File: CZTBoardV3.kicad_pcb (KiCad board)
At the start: 2 copper layers, 80 x 100 mm, 34 parts, among them IC1 LD117AS, IC2 LD117AS, U1 ORBOTECH_OMS40G256, U2 DS90LV031, U3 DS90LV032, X1 W237-102, X2 W237-102, X3 W237-103, X4 W237-102, X5 W237-102

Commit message: new layout
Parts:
- removed the X1 at (105.4, 41.9)

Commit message: added side panel
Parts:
- removed C5: C5, CZTBoardV3:C0805K
- removed R7, R8: 0, CZTBoardV3:R1206
- added C10: 0.0123uF, CZTBoardV3:C0805K, F.Cu at (144.5, 64.5)
- added C11: 0.1uF, CZTBoardV3:C0805K, F.Cu at (135.9, 66.6)
- added C12: 0.1uF, CZTBoardV3:C0805K, F.Cu at (149.1, 52.9)
- added C13: 4.7uF, CZTBoardV3:C0805K, F.Cu at (148.9, 55.9)
- added C14: 4.7uF, CZTBoardV3:C0805K, F.Cu at (142.9, 61.9)
- added C15: 0.1uF, CZTBoardV3:C0805K, F.Cu at (140.2, 65.8)
- added C16: 0.1uF, CZTBoardV3:C0805K, F.Cu at (153.4, 52.9)
- added C17: 4.7uF, CZTBoardV3:C0805K, F.Cu at (147.2, 59.3)
- added C18: 4.7uF, CZTBoardV3:C0805K, F.Cu at (153.2, 55.5)
- added C19: 0.1uF, CZTBoardV3:C0805K, F.Cu at (147.2, 61.9)
- added C20: 0.1uF, CZTBoardV3:C0805K, F.Cu at (142.9, 59.3)
- added C21: 4.7uF, CZTBoardV3:C0805K, F.Cu at (151.5, 58.5)
- added C22: 4.7uF, CZTBoardV3:C0805K, F.Cu at (151.5, 61.1)
- added L1: 40uH, Inductor_SMD:L_1206_3216Metric, F.Cu at (137.9, 62.8)
- added L2: 100uH, Inductor_SMD:L_1206_3216Metric, F.Cu at (137.9, 59.3)
- added L3: 100uH, Inductor_SMD:L_1206_3216Metric, F.Cu at (143.9, 56.3)
- added R20: 470k, CZTBoardV3:R1206, F.Cu at (138.0, 56.1)
- added R21: 10E, CZTBoardV3:R1206, F.Cu at (144.0, 53.1)
- added R22: 10E, CZTBoardV3:R1206, F.Cu at (138.0, 53.1)
- added R23: 10E, CZTBoardV3:R1206, F.Cu at (130.8, 66.8)
- added U4: DHT11, Sensor:Aosong_DHT11_5.5x12.0_P2.54mm, F.Cu at (131.5, 54.7)
- R5: value 0 -> 0E
- moved R5 65.4 mm to (163.8, 67.3), turned to 0 degrees
- moved C2 2.54 mm to (154.7, 115.1)
- moved R12 2.54 mm to (175.6, 126.3)
- moved R14 2.54 mm to (130.6, 119.5)
- moved R17 2.54 mm to (166.4, 100.7)
- moved R2 2.54 mm to (171.7, 121.7)
- moved X4 2.54 mm to (155.3, 143.6)
- moved R11 2.54 mm to (120.4, 137.7)
- moved U1 2.54 mm to (107.7, 71.4)
- moved C3 2.54 mm to (169.7, 107.3)
- moved C4 2.54 mm to (137.5, 113.6)
- moved C6 2.54 mm to (117.9, 114.4)
- moved IC1 2.54 mm to (133.6, 131.8)
- moved IC2 2.54 mm to (121.3, 123.3)
- moved R1 2.54 mm to (147.4, 118.9)
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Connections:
- R5 pad 1: Net-(IC1-Pad4) -> /AVFE_LDO
- R5 pad 2: VCC -> Net-(C12-Pad1)
- X1 pad 1: GND -> AGND
- X1 pad 2: /CZT_VIN -> /VIN5V
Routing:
- net AGND: track 80.2 -> 303.1 mm, vias 0 -> 8
- net DGND: track 186.6 -> 0.00 mm, vias 7 -> 0
- net GND: track 36.3 -> 0.00 mm, vias 5 -> 0
- net VCC: track 49.2 -> 62.4 mm
- net Net-(IC1-Pad4): track 13.2 -> 0.00 mm
- net /VIN5V: track 0.00 -> 10.1 mm, vias 0 -> 1
- net /CZT_VIN: track 10.1 -> 0.00 mm, vias 1 -> 0
- removed copper zone on B.Cu, net GND
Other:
- board text added: "08/2021 AG"
- board text removed: "MAR 2021 ~HSB"

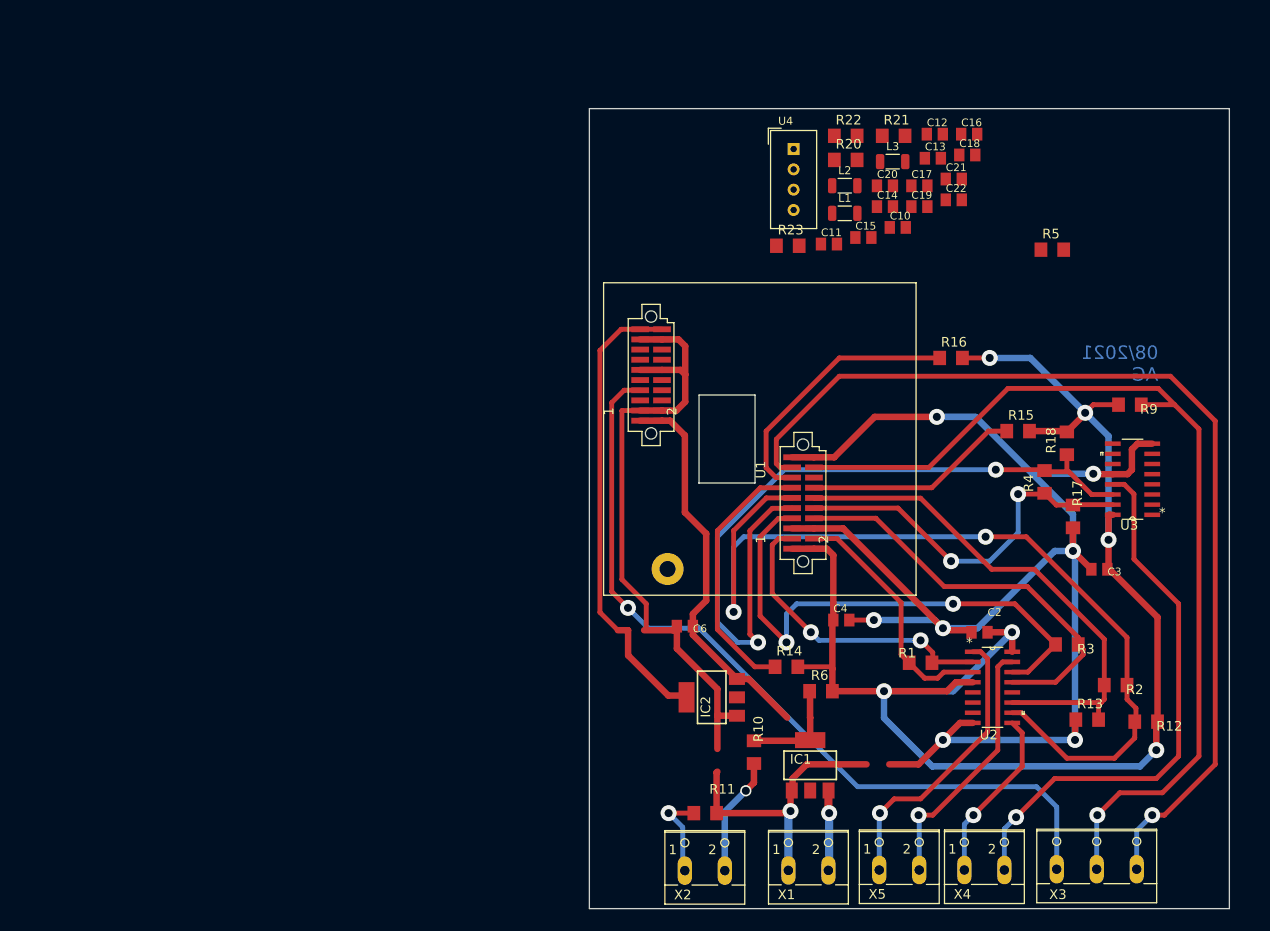
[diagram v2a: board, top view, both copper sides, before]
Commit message: airwire removal time
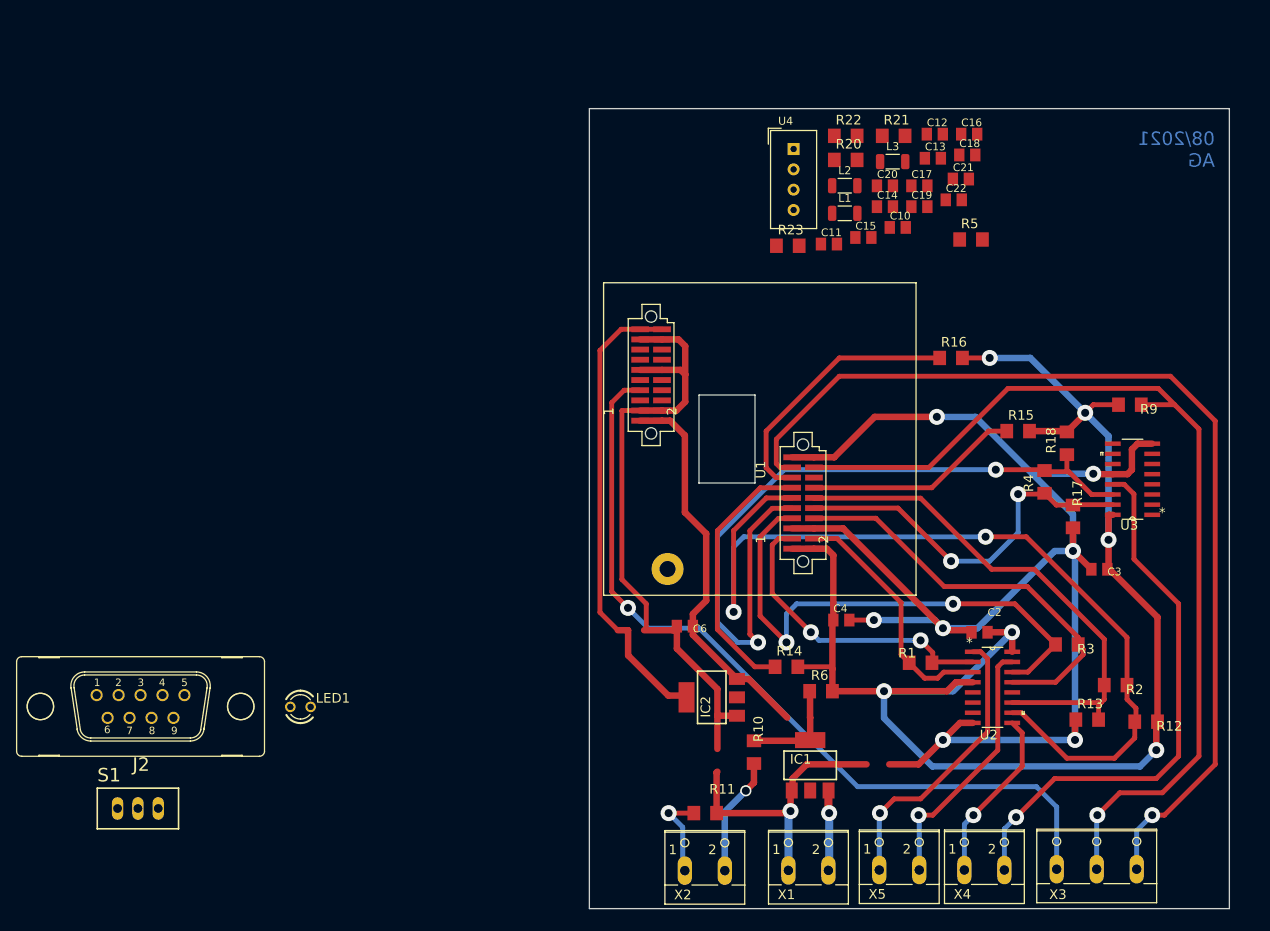
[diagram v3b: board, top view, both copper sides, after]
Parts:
- added J2: DB9_Male, CZTBoardV3:M09V, F.Cu at (49.9, 124.4)
- added LED1: LED, CZTBoardV3:LED3MM, F.Cu at (69.8, 124.5)
- added S1: TL32PO, CZTBoardV3:TL3XPO, F.Cu at (49.5, 137.2)
- moved R5 10.2 mm to (153.7, 66.0)
- moved C21 0.89 mm to (152.4, 58.5)
